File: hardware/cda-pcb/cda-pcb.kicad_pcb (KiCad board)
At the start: 4 copper layers, 112 x 127 mm, 190 parts, among them J1 ICD15S13E4GX00LF, J2 ICD15S13E4GX00LF, J3 ICD15S13E4GX00LF, J4 ICD15S13E4GX00LF, J6 Conn_01x06, P1 0022272021, U1 ADS124S08IRHBT, U10 SN74AHCT125RGYR, U2 ADS124S08IRHBT, U3 ADS124S08IRHBT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

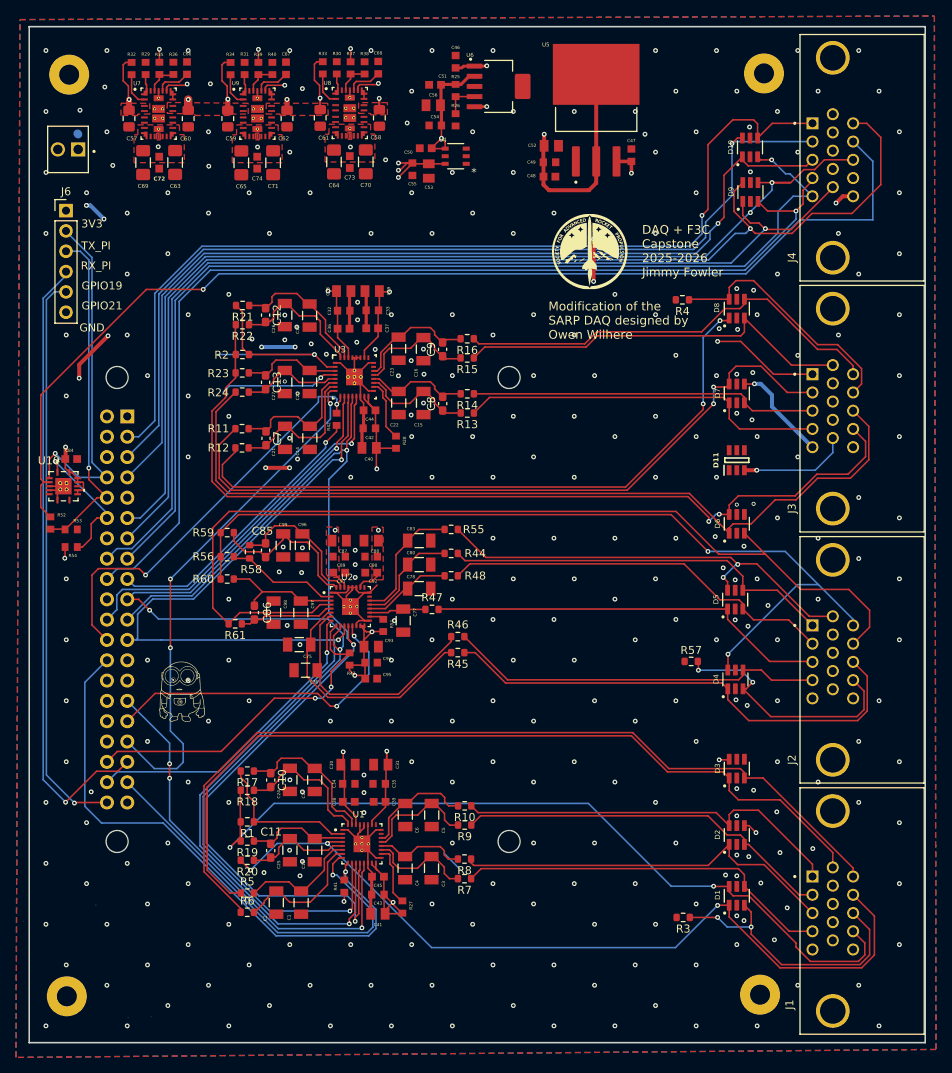
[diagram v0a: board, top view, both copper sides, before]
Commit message: potentially done with DRC
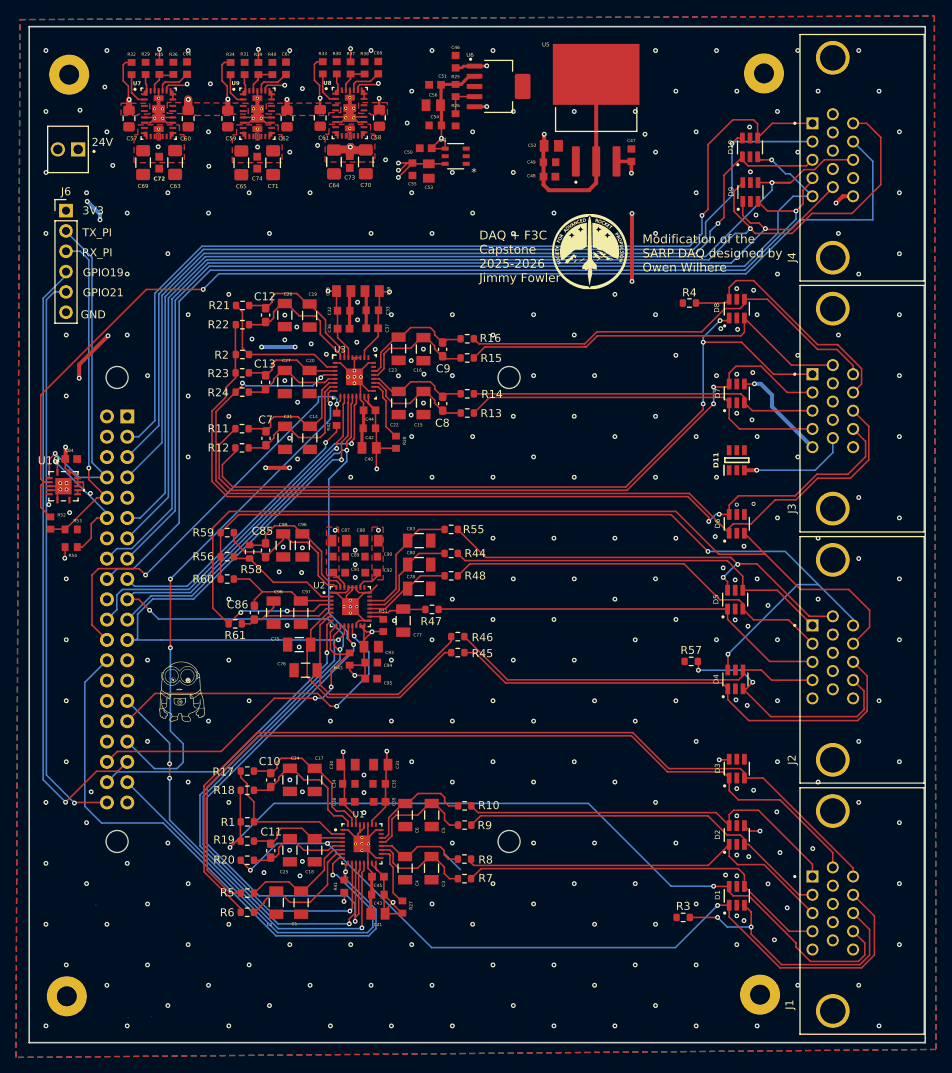
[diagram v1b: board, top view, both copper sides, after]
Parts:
- moved R4 0.96 mm to (148.8, 67.2)
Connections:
- U7 pad 32: (no net) -> GND
- U7 pad 35: (no net) -> GND
- U7 pad 36: (no net) -> GND
- U8 pad 31: (no net) -> +11V
- U8 pad 32: (no net) -> GND
- U8 pad 35: (no net) -> GND
- U8 pad 36: (no net) -> GND
- U9 pad 31: (no net) -> +6V
- U9 pad 32: (no net) -> GND
- U9 pad 35: (no net) -> GND
- U9 pad 36: (no net) -> GND
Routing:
- net GND: track 85.2 -> 110.9 mm, vias 309 -> 313
- net /IDAC1_1: track 30.3 -> 18.2 mm, vias 1 -> 0
- net +6V: track 66.2 -> 73.6 mm
- net +11V: track 45.1 -> 50.6 mm
- net +10Vs: track 106.1 -> 102.2 mm
- net Net-(U2-AIN2): track 12.3 -> 14.6 mm
- net /LS1_SIG-: track 95.7 -> 97.5 mm
- net +3.3V: track 250.9 -> 249.7 mm
- net /IDAC2_1: track 122.4 -> 121.4 mm, vias 1 -> 2
- net /RTD1_L3: track 31.4 -> 30.7 mm
- net /IDAC2_3: vias 0 -> 2
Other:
- board text added: "24V"

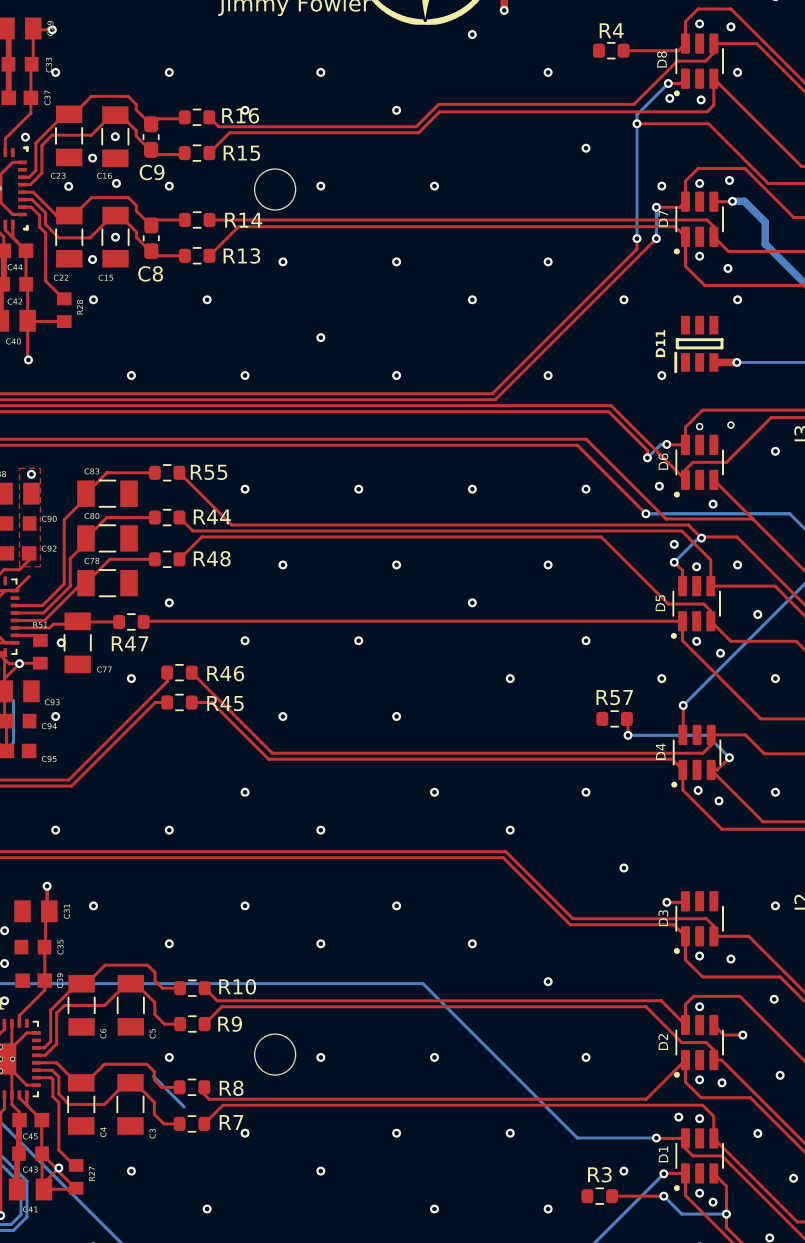
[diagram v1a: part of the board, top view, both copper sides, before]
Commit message: changes for ease of assembly
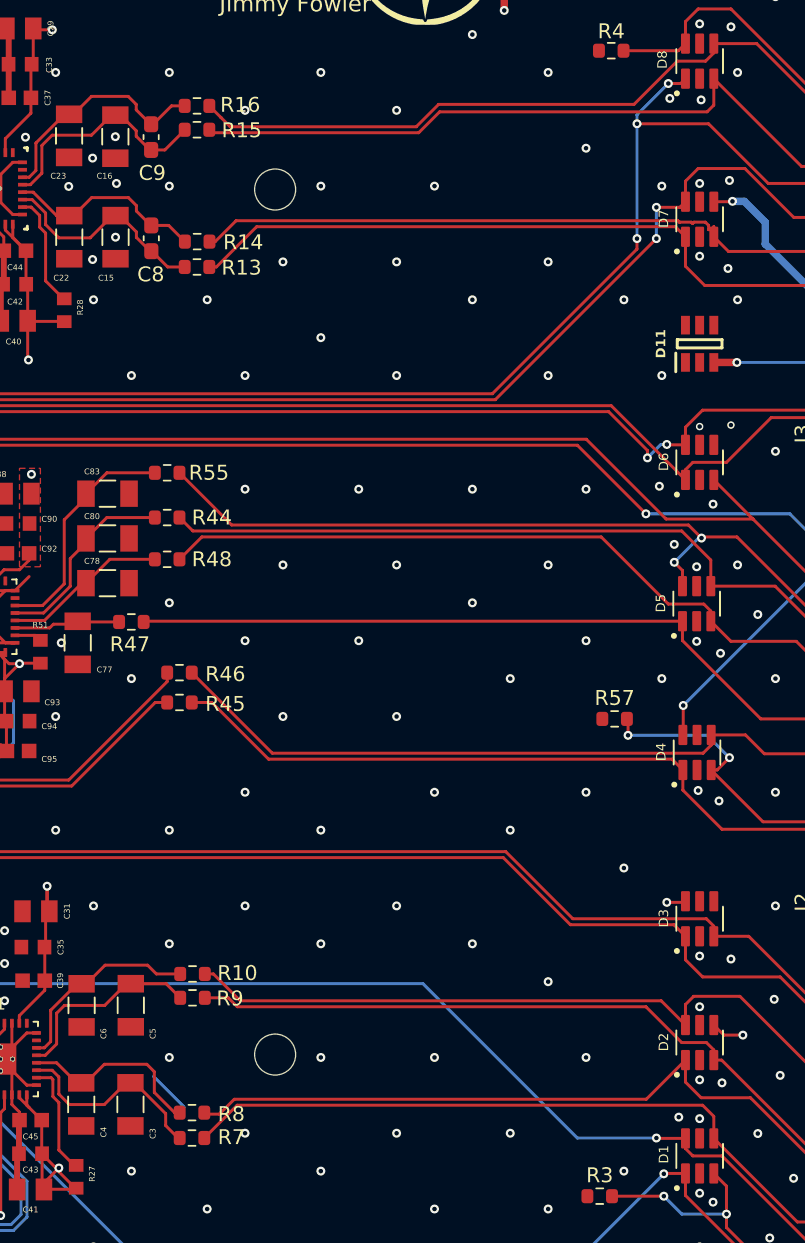
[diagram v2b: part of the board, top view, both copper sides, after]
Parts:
- moved R9 1.76 mm to (120.8, 130.7)
- moved R8 1.70 mm to (120.7, 138.4)
- moved R15 1.56 mm to (121.1, 72.5)
- moved R14 1.45 mm to (121.1, 80.0)
- moved R10 0.96 mm to (120.8, 129.1)
- moved R7 0.94 mm to (120.7, 140.1)
- moved R16 0.76 mm to (121.1, 70.9)
- moved R13 0.75 mm to (121.1, 81.7)
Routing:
- net Net-(U1-GPIO2_AIN10): track 11.2 -> 12.4 mm
- net /LS2_SIG-: track 43.6 -> 44.6 mm
- net Net-(U1-GPIO1_AIN9): track 14.1 -> 13.2 mm
- net Net-(U1-GPIO0_AIN8): track 13.3 -> 12.6 mm
- net Net-(U3-GPIO1_AIN9): track 14.8 -> 15.3 mm
- net /LS3_SIG+: track 50.4 -> 49.9 mm

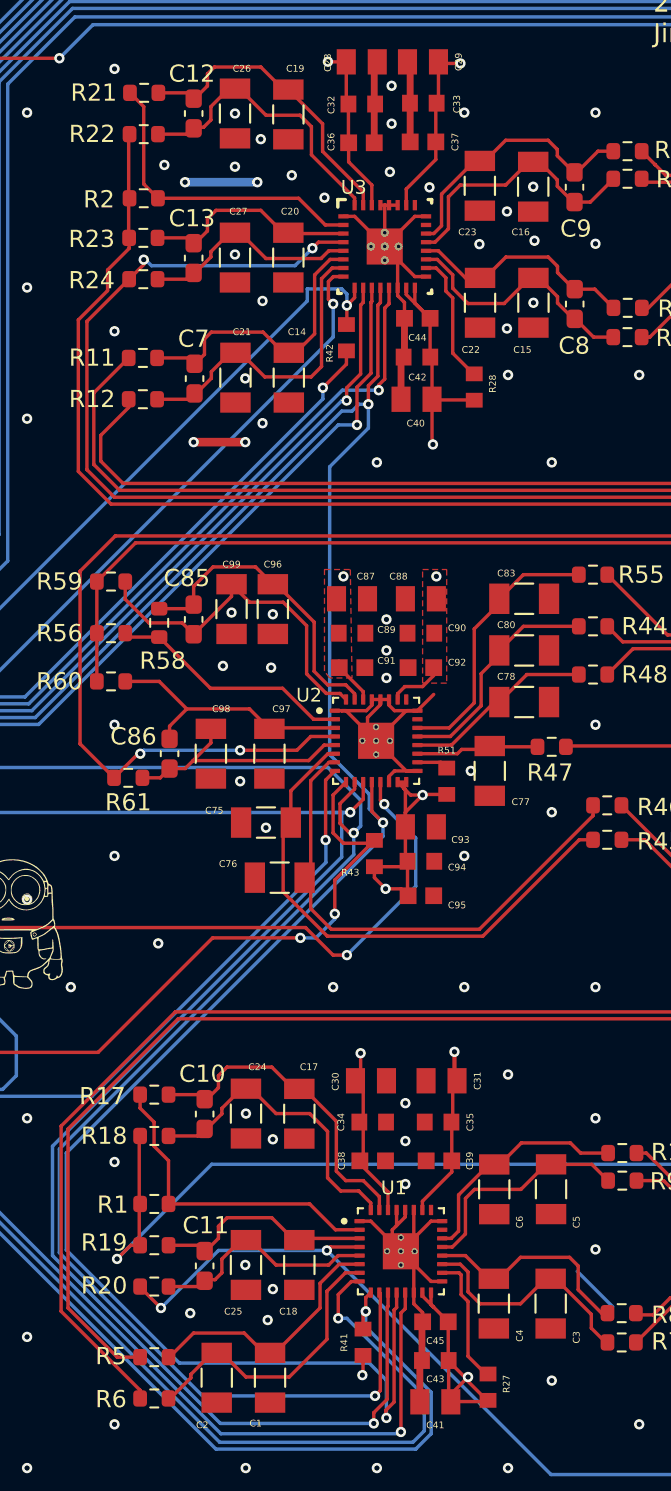
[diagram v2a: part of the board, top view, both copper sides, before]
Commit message: added 3d models
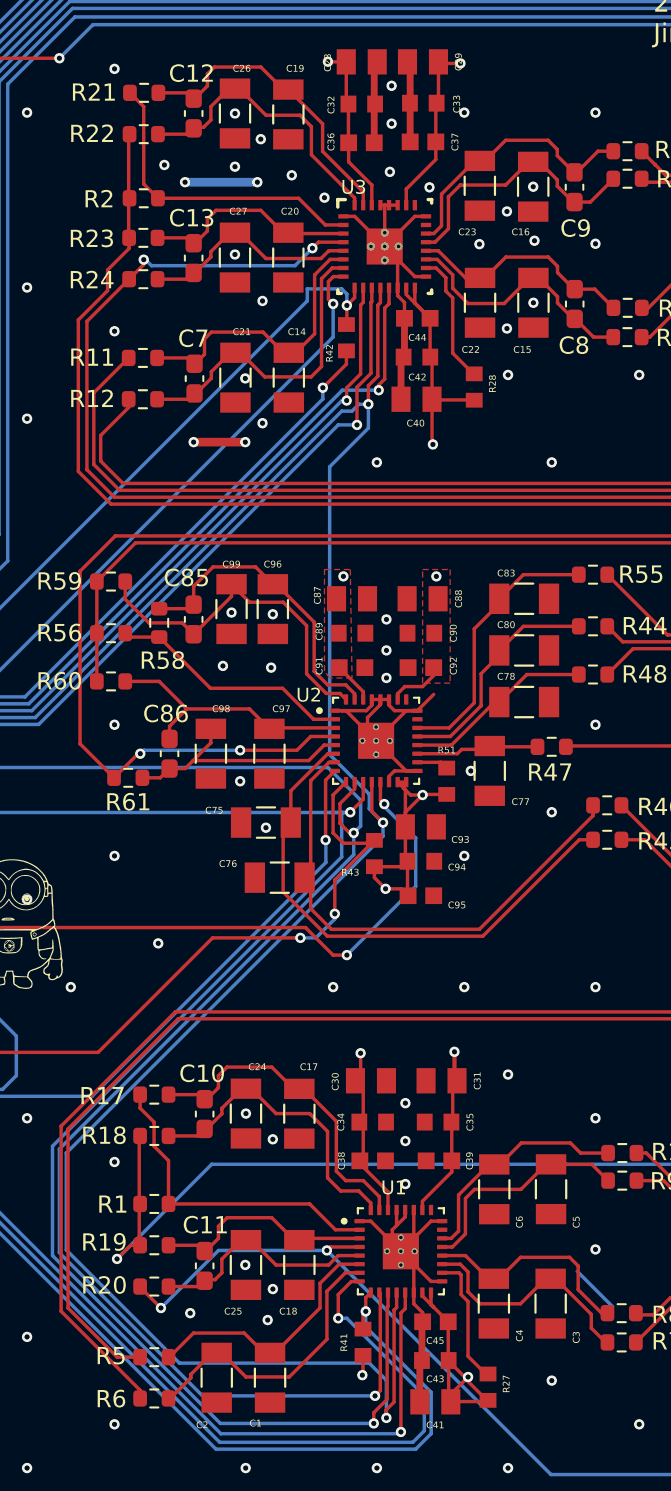
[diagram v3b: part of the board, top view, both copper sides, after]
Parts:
- moved C88 0.10 mm to (109.2, 96.9)
